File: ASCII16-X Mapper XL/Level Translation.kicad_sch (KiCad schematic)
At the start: 23 parts, among them U2 74LVC32A, U3 74LVC541A, U4 74LVC541A, U5 TLV1117LV33, U6 74LVC541A, U7 74HCT541

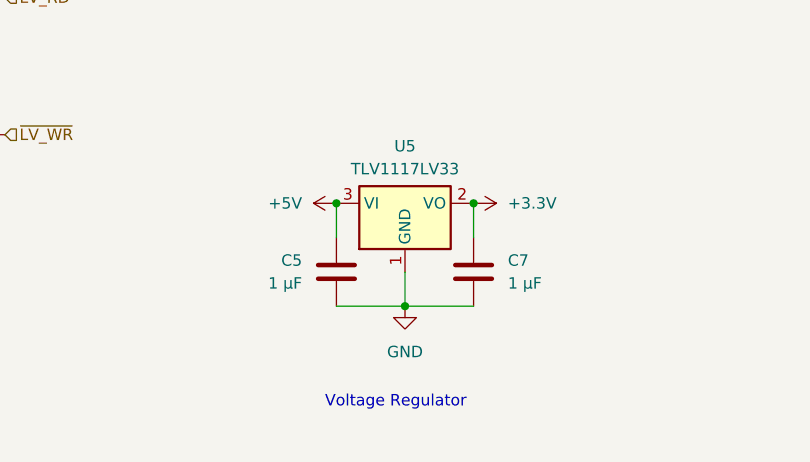
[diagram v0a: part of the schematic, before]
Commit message: Change LDO input / output caps to 10 µF.
The TLV1117LV33’s datasheet specifies input & output caps of 1 µF.
However the TLV1117LV33EVM-714 evaluation board has 10 µF caps, quote:

> The input and output capacitors for the TLV1117LVxx need be 0.4 μF (effective
> minimum) for stability; however, for conservative design practice accounting
> for widely varying noise environments, and dynamic line/load conditions, a
> 10-μF capacitor has been employed at the input and output ports.

See https://www.ti.com/lit/pdf/slvu449

Thanks to Wlcracks for the advice.
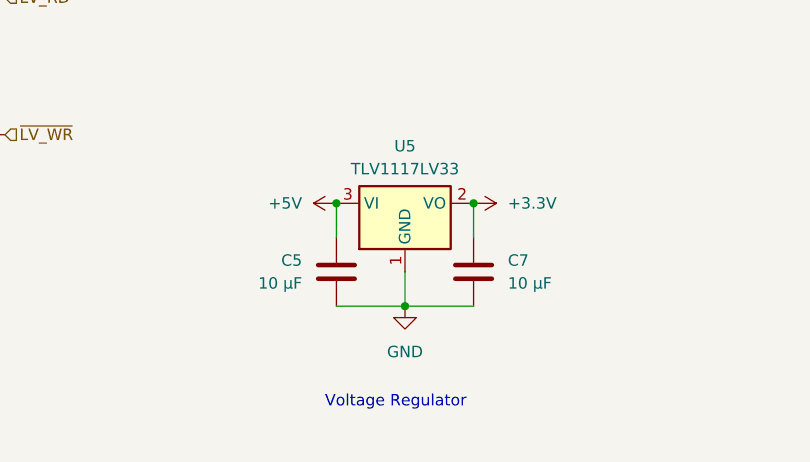
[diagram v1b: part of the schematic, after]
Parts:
- C5, C7: value 1 µF -> 10 µF; MPN CL21B105KAFNNNE -> CL21A106KOQNNNE
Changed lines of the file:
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@@
 			)
 		)
-		(property "Value" "1 µF"
+		(property "Value" "10 µF"
 			(at 137.16 177.8 0)
 			(effects
@@
 			)
 		)
-		(property "Description" "CAP CER 1UF 25V X7R 10% 0805"
+		(property "Description" "CAP CER 10UF 16V X5R 10% 0805"
 			(at 140.97 176.53 0)
 			(effects
@@
 			)
 		)
-		(property "MPN" "CL21B105KAFNNNE"
+		(property "MPN" "CL21A106KOQNNNE"
 			(at 140.97 176.53 0)
 			(effects
@@
 			)
 		)
-		(property "Value" "1 µF"
+		(property "Value" "10 µF"
 			(at 160.02 177.8 0)
 			(effects
@@
 			)
 		)
-		(property "Description" "CAP CER 1UF 25V X7R 10% 0805"
+		(property "Description" "CAP CER 10UF 16V X5R 10% 0805"
 			(at 156.21 176.53 0)
 			(effects
@@
 			)
 		)
-		(property "MPN" "CL21B105KAFNNNE"
+		(property "MPN" "CL21A106KOQNNNE"
 			(at 156.21 176.53 0)
 			(effects

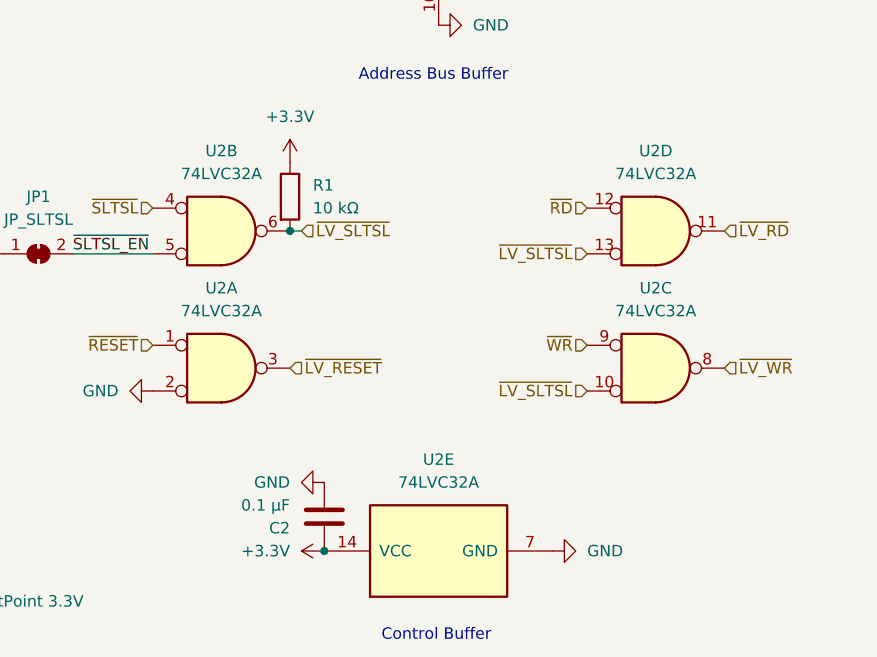
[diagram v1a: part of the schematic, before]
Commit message: Increase noise tolerance on control signals.
Replacing the SN74LVC32A with a SN74LVC7032A with Schmitt inputs.

When the control lines are noisy, if the noise is so bad that it goes under the
threshold of 2 V logic high momentarily, this can produce false control signals.
Because the LVC series of logic gates have a fast propagation time they are much
more sensitive to this than LS or HCT series parts.

This has been observed with the MK 3.0 slot expander, whose 75 cm long ribbon
cable picks up a lot of noise, but it doesn’t buffer the signals. Under certain
conditions (unpowered, several other carts plugged in) the control signals can
dip under the threshold during Flash operations. This particularly affects the
/RESET, /RD and /WR lines; /SLTSL is locally generated and thus not affected.

The /RD and /WR signals are gated by /SLTSL so it is not an issue for them,
however a false transient /RESET signal will cause the mapper registers to
reset. The Flash chip is unaffected since reset must be held for 200 ns.

The SN74LVC7032A is a fairly new variant of the SN74LVC32A with Schmitt trigger
inputs. The hysteresis makes it more tolerant of noise. Tests have shown it
(almost) entirely eliminates the issue.
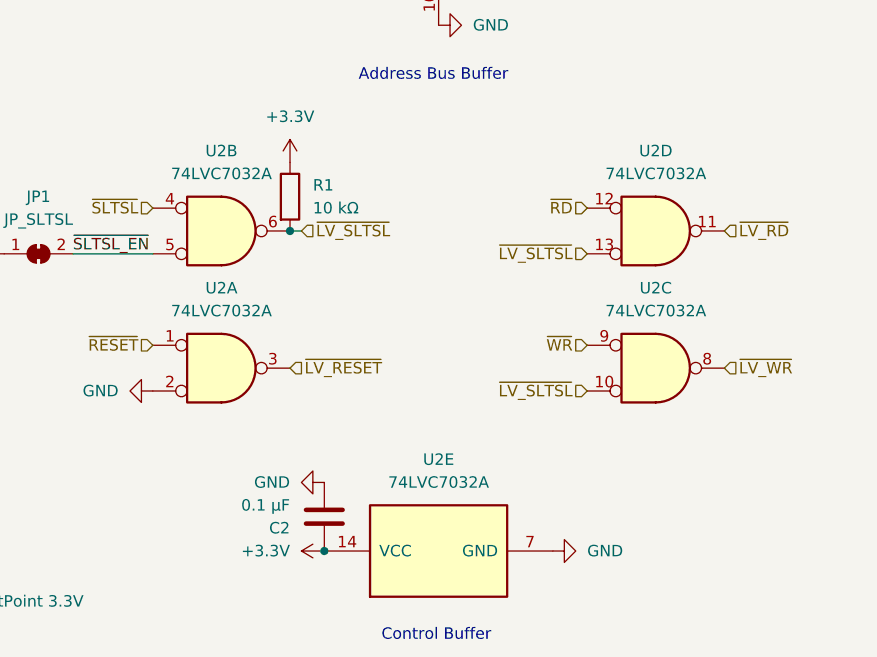
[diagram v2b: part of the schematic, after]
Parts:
- U2: value 74LVC32A -> 74LVC7032A; MPN SN74LVC32APWR -> SN74LVC7032APWR; Substitutes Texas Instruments SN74LVC32APWT, Nexperia 74LVC32APW,118 -> Texas Instruments SN74LVC32APWR, SN74LVC32APWT, Nexperia 74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
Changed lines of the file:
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@@
 			)
 		)
-		(property "Value" "74LVC32A"
+		(property "Value" "74LVC7032A"
 			(at 96.52 139.7 0)
 			(effects
@@
 			)
 		)
-		(property "Datasheet" "http://www.ti.com/lit/gpn/SN74LVC32A"
+		(property "Datasheet" "http://www.ti.com/lit/gpn/SN74LVC7032A"
 			(at 96.52 146.05 0)
 			(effects
@@
 			)
 		)
-		(property "Description" "IC GATE OR 4CH 2-INP 14TSSOP"
+		(property "Description" "IC GATE OR SCHMITT 4CH 2-INP 14TSSOP"
 			(at 96.52 146.05 0)
 			(effects
@@
 			)
 		)
-		(property "MPN" "SN74LVC32APWR"
+		(property "MPN" "SN74LVC7032APWR"
 			(at 96.52 146.05 0)
 			(effects
@@
 			)
 		)
-		(property "Substitutes" "Texas Instruments SN74LVC32APWT, Nexperia 74LVC32APW,118"
+		(property "Substitutes" "Texas Instruments SN74LVC32APWR, SN74LVC32APWT, Nexperia 74LVC32APW,118"
 			(at 96.52 146.05 0)
 			(effects
@@
 			)
 		)
-		(property "Value" "74LVC32A"
+		(property "Value" "74LVC7032A"
 			(at 48.26 139.7 0)
 			(effects
@@
 			)
 		)
-		(property "Datasheet" "http://www.ti.com/lit/gpn/SN74LVC32A"
+		(property "Datasheet" "http://www.ti.com/lit/gpn/SN74LVC7032A"
 			(at 48.26 146.05 0)
 			(effects
@@
 			)
 		)
-		(property "Description" "IC GATE OR 4CH 2-INP 14TSSOP"
+		(property "Description" "IC GATE OR SCHMITT 4CH 2-INP 14TSSOP"
 			(at 48.26 146.05 0)
 			(effects
@@
 			)
 		)
-		(property "MPN" "SN74LVC32APWR"
+		(property "MPN" "SN74LVC7032APWR"
 			(at 48.26 146.05 0)
 			(effects
@@
 			)
 		)
-		(property "Substitutes" "Texas Instruments SN74LVC32APWT, Nexperia 74LVC32APW,118"
+		(property "Substitutes" "Texas Instruments SN74LVC32APWR, SN74LVC32APWT, Nexperia 74LVC32APW,118"
 			(at 48.26 146.05 0)
 			(effects
@@
 			)
 		)
-		(property "Value" "74LVC32A"
+		(property "Value" "74LVC7032A"
 			(at 72.39 173.99 90)
 			(effects
@@
 			)
 		)
-		(property "Datasheet" "http://www.ti.com/lit/gpn/SN74LVC32A"
+		(property "Datasheet" "http://www.ti.com/lit/gpn/SN74LVC7032A"
 			(at 72.39 181.61 0)
 			(effects
@@
 			)
 		)
-		(property "Description" "IC GATE OR 4CH 2-INP 14TSSOP"
+		(property "Description" "IC GATE OR SCHMITT 4CH 2-INP 14TSSOP"
 			(at 72.39 181.61 0)
 			(effects
@@
 			)
 		)
-		(property "MPN" "SN74LVC32APWR"
+		(property "MPN" "SN74LVC7032APWR"
 			(at 72.39 181.61 0)
 			(effects
@@
 			)
 		)
-		(property "Substitutes" "Texas Instruments SN74LVC32APWT, Nexperia 74LVC32APW,118"
+		(property "Substitutes" "Texas Instruments SN74LVC32APWR, SN74LVC32APWT, Nexperia 74LVC32APW,118"
 			(at 72.39 181.61 0)
 			(effects
@@
 			)
 		)
-		(property "Value" "74LVC32A"
+		(property "Value" "74LVC7032A"
 			(at 96.52 154.94 0)
 			(effects
@@
 			)
 		)
-		(property "Datasheet" "http://www.ti.com/lit/gpn/SN74LVC32A"
+		(property "Datasheet" "http://www.ti.com/lit/gpn/SN74LVC7032A"
 			(at 96.52 161.29 0)
 			(effects
@@
 			)
 		)
-		(property "Description" "IC GATE OR 4CH 2-INP 14TSSOP"
+		(property "Description" "IC GATE OR SCHMITT 4CH 2-INP 14TSSOP"
 			(at 96.52 161.29 0)
 			(effects
@@
 			)
 		)
-		(property "MPN" "SN74LVC32APWR"
+		(property "MPN" "SN74LVC7032APWR"
 			(at 96.52 161.29 0)
 			(effects
@@
 			)
 		)
-		(property "Substitutes" "Texas Instruments SN74LVC32APWT, Nexperia 74LVC32APW,118"
+		(property "Substitutes" "Texas Instruments SN74LVC32APWR, SN74LVC32APWT, Nexperia 74LVC32APW,118"
 			(at 96.52 161.29 0)
 			(effects
@@
 			)
 		)
-		(property "Value" "74LVC32A"
+		(property "Value" "74LVC7032A"
 			(at 48.26 154.94 0)
 			(effects
@@
 			)
 		)
-		(property "Datasheet" "http://www.ti.com/lit/gpn/SN74LVC32A"
+		(property "Datasheet" "http://www.ti.com/lit/gpn/SN74LVC7032A"
 			(at 48.26 161.29 0)
 			(effects
@@
 			)
 		)
-		(property "Description" "IC GATE OR 4CH 2-INP 14TSSOP"
+		(property "Description" "IC GATE OR SCHMITT 4CH 2-INP 14TSSOP"
 			(at 48.26 161.29 0)
 			(effects
@@
 			)
 		)
-		(property "MPN" "SN74LVC32APWR"
+		(property "MPN" "SN74LVC7032APWR"
 			(at 48.26 161.29 0)
 			(effects
@@
 			)
 		)
-		(property "Substitutes" "Texas Instruments SN74LVC32APWT, Nexperia 74LVC32APW,118"
+		(property "Substitutes" "Texas Instruments SN74LVC32APWR, SN74LVC32APWT, Nexperia 74LVC32APW,118"
 			(at 48.26 161.29 0)
 			(effects
